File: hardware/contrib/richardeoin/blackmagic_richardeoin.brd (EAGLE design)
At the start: 33 parts, among them IC1 STM32F_48PIN, IC2 TXS0108, IC3 TLV70033DCK, Q1 IRLML5103, Y1 8MHz

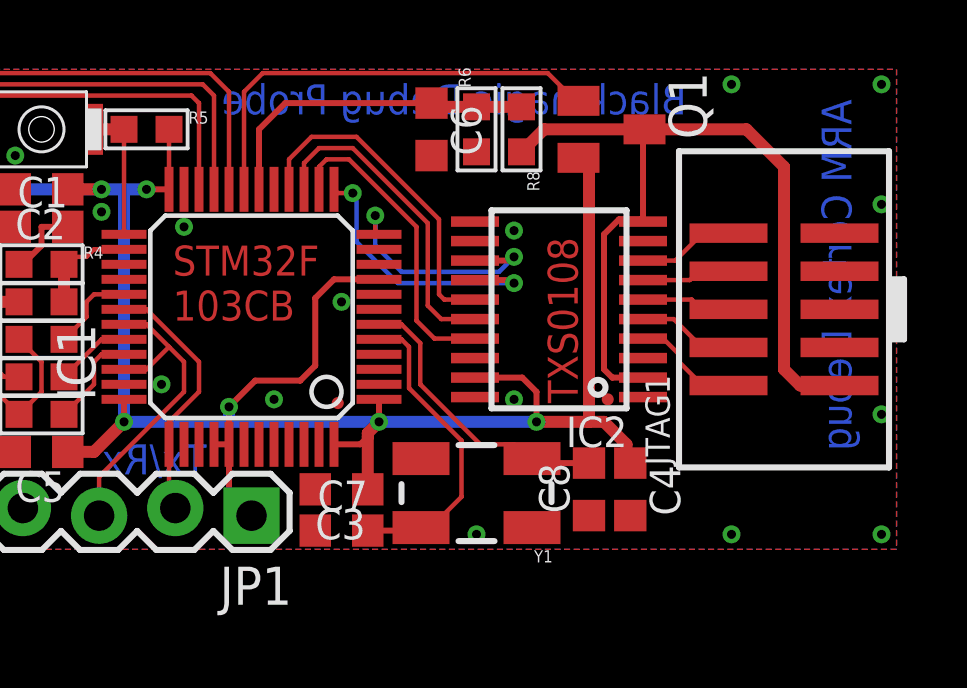
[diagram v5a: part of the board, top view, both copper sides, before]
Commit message: Added switch on BOOT0
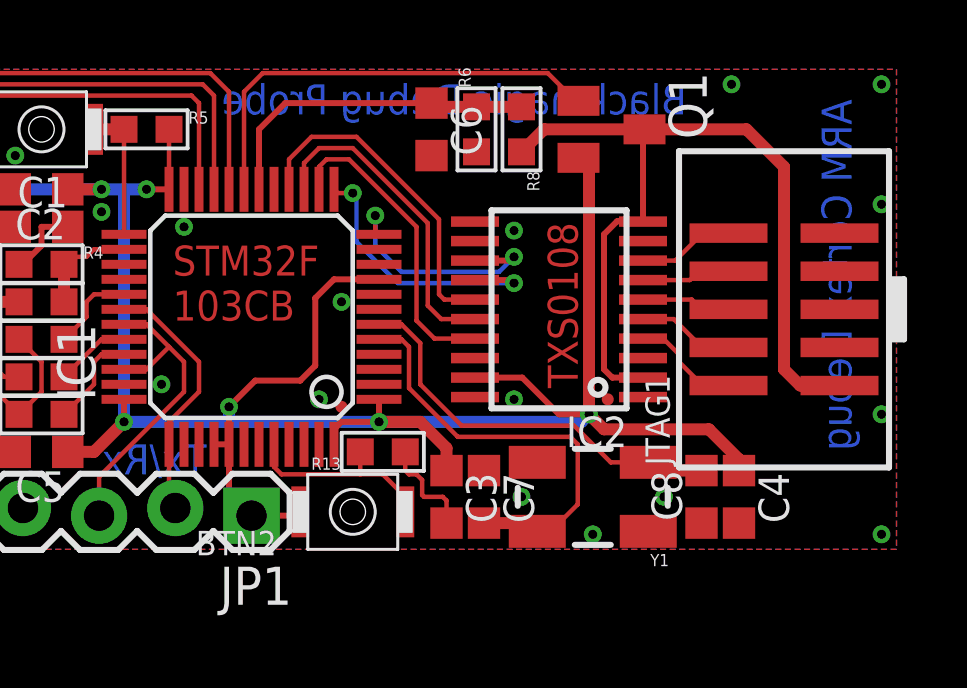
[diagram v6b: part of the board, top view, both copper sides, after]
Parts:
- added BTN2: SPST.B3U-1000P(M)-B, omron:B3U-1000P(M)-B
- added R13: 10K, microbuilder:0603-MINI
- moved C7 4.88 mm to (26.2, 1.75), turned to 270 degrees
- moved Y1 3.88 mm to (29.9, 1.75)
- moved C8 3.76 mm to (33.5, 1.75)
- moved C4 3.63 mm to (34.8, 1.75)
- moved C3 3.51 mm to (25.0, 1.75), turned to 270 degrees
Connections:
- new net BOOT0: BTN2.1, IC1.44, R13.2
- net 3.3V: now also BTN2.2
- net GND: now also R13.1; no longer IC1.44
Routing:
- net 3.3V: track 74.3 -> 82.6 mm
- net BOOT0: track 0.00 -> 6.79 mm
- net OSC_IN: track 10.4 -> 14.5 mm
- net LPC_XTAL2: track 9.70 -> 13.6 mm
- net GND: track 4.09 -> 7.54 mm, vias 21 -> 22
